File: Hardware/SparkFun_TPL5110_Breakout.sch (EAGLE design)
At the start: 1 part

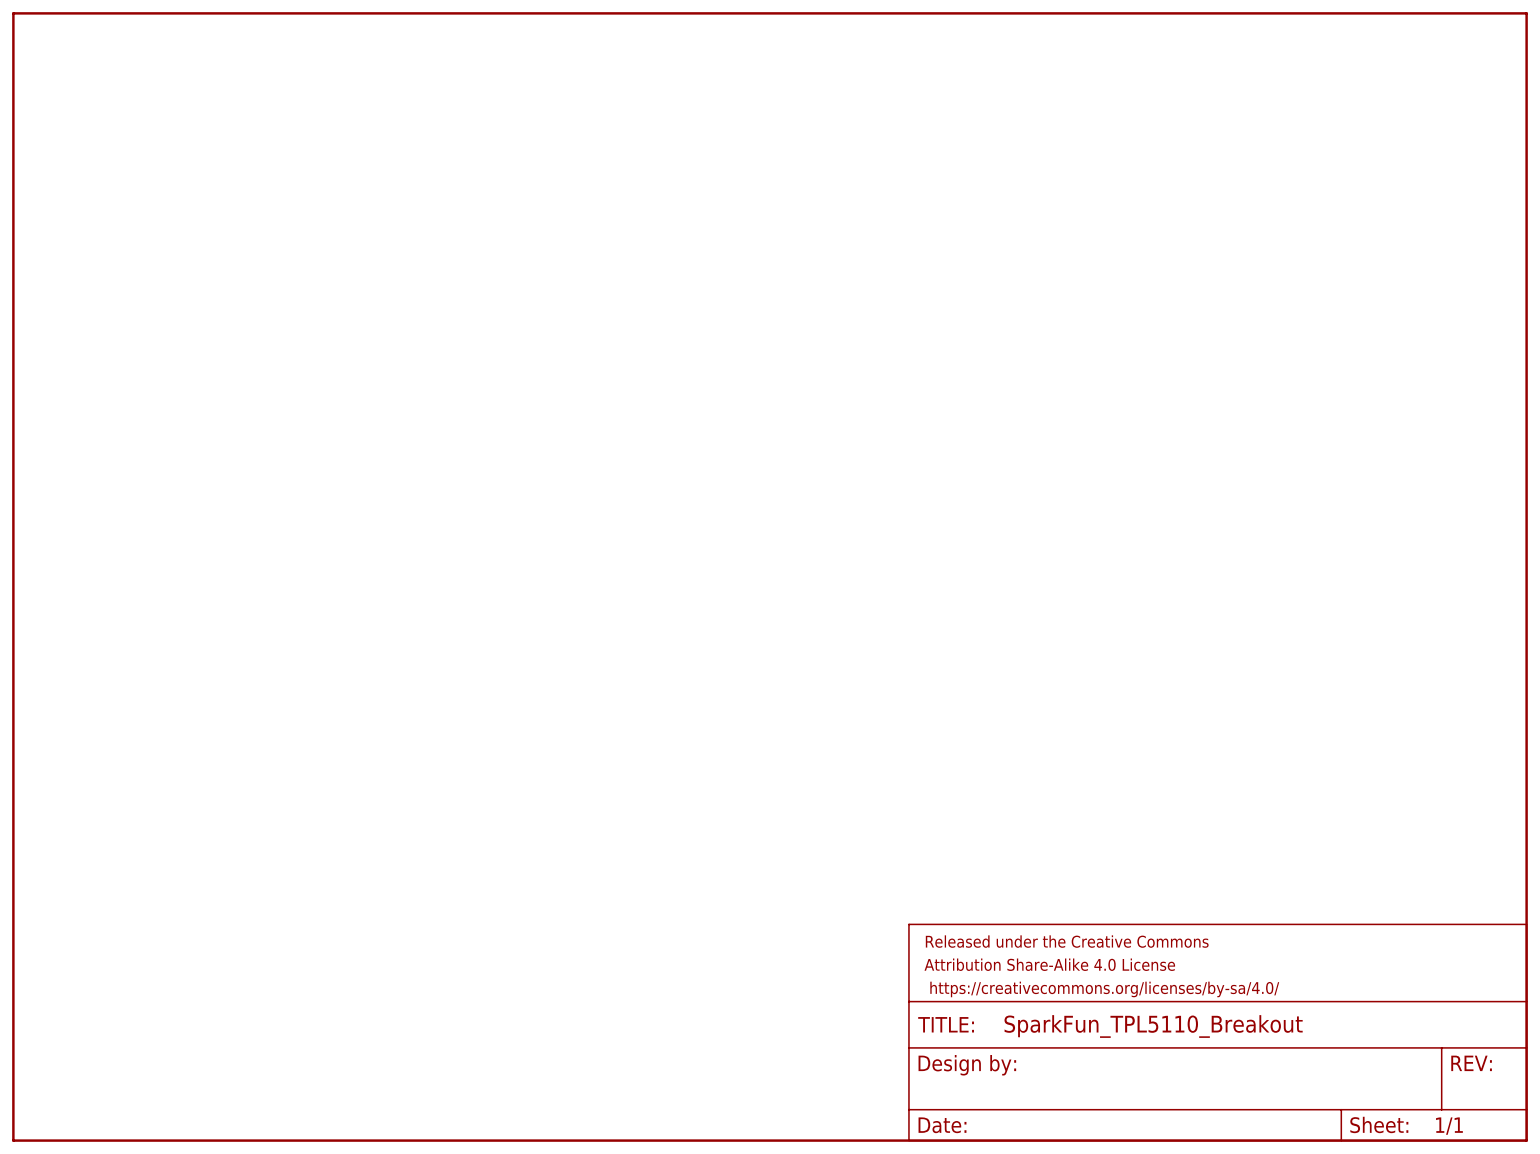
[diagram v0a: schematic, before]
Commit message: Completes schematic and board design, adds buzzard labels
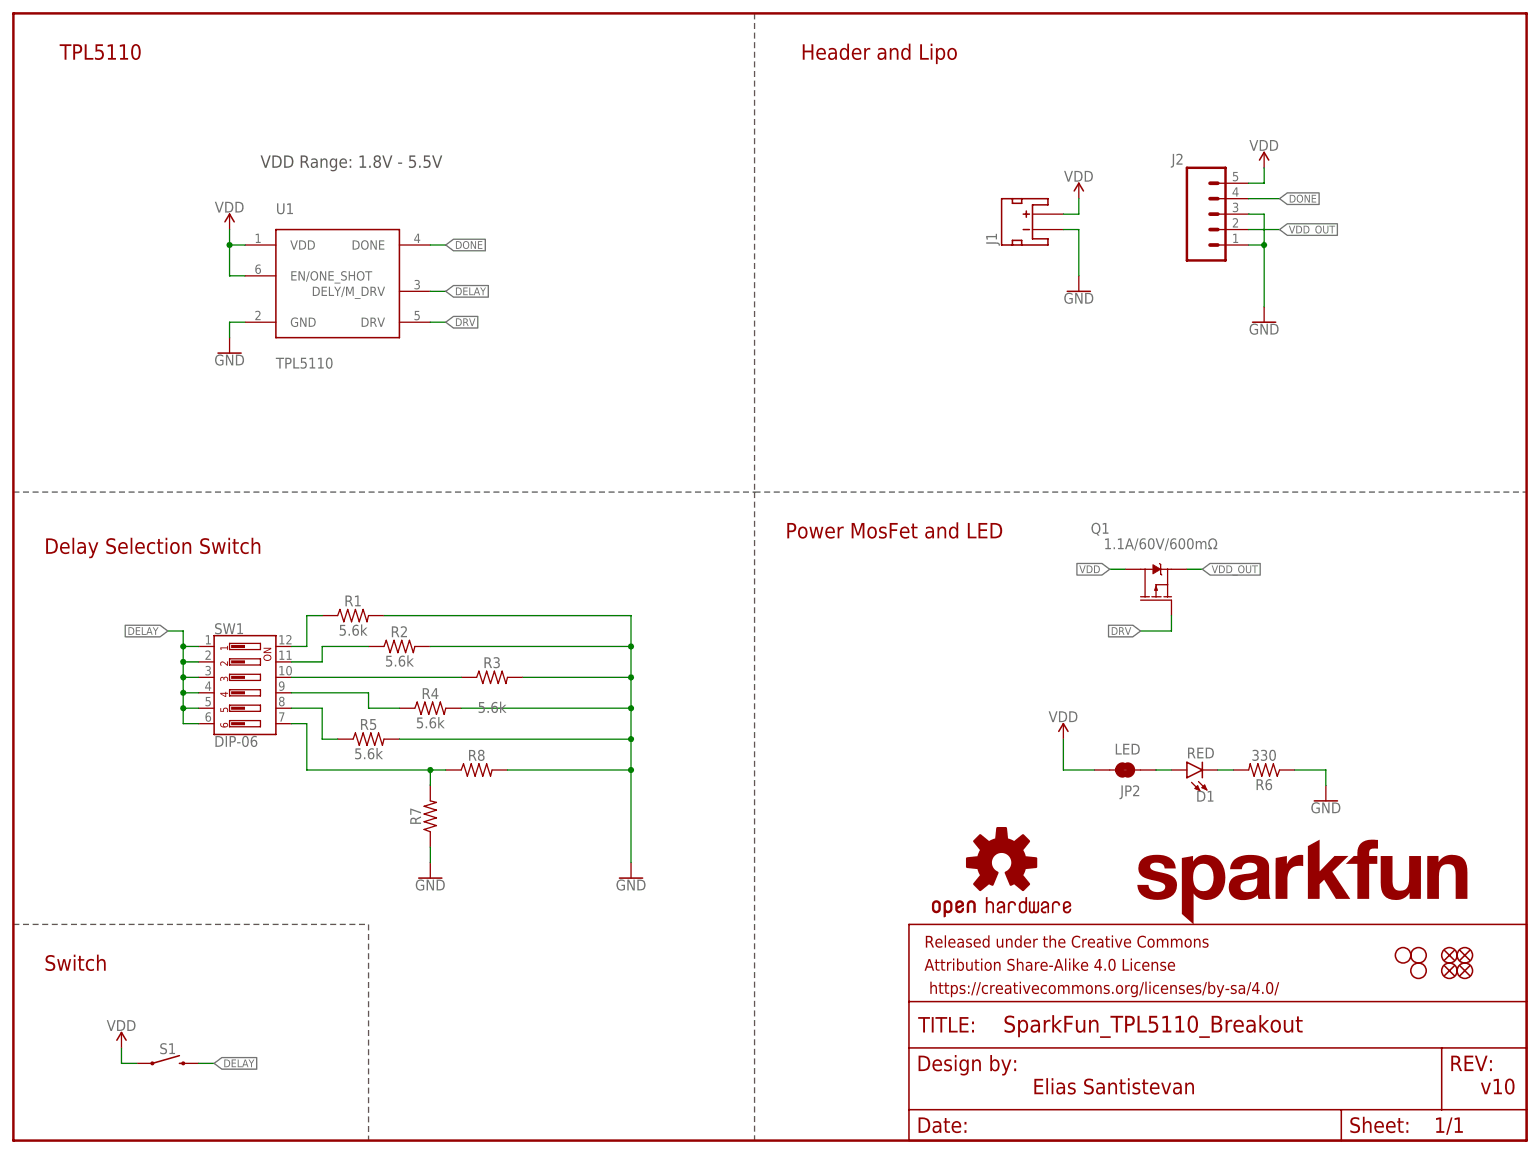
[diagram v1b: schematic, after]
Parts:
- added D1: RED, SparkFun-LED:LED-RED0603
- added FD1, FD2, FD3, FD4: FIDUCIALUFIDUCIAL, SparkFun-Aesthetics:FIDUCIALUFIDUCIAL
- added H1, H2, H4: STAND-OFFTIGHT, SparkFun-Hardware:STAND-OFFTIGHT
- added J1: (no value), SparkFun-Connectors:JST_2MM_MALE
- added J2: (no value), SparkFun-Connectors:CONN_05NO_SILK
- added JP2: LED, SparkFun-Jumpers:JUMPER-SMT_2_NC_TRACE_SILK
- added LOGO1: SFE_LOGO_NAME.1_INCH, SparkFun-Aesthetics:SFE_LOGO_NAME.1_INCH
- added LOGO2: OSHW-LOGOS, SparkFun-Aesthetics:OSHW-LOGOS
- added Q1: 1.1A/60V/600mΩ, SparkFun-DiscreteSemi:MOSFET_PCH-SI2309DS
- added R1, R2, R3, R4, R5: 5.6k, SparkFun-Resistors:5.6KOHM-0603-1/10W-1%
- added R6: 330, SparkFun-Resistors:330OHM-0603-1/10W-1%
- added R7: (no value), SparkFun-Resistors:RESISTOR0603
- added R8: (no value), SparkFun-Resistors:RESISTORAXIAL-0.3
- added S1: MOMENTARY-SWITCH-SPST-SMD-5.2MM-TALL, SparkFun-Switches:MOMENTARY-SWITCH-SPST-SMD-5.2MM-TALL
- added SW1: DIP-06, SparkFun-Switches:DIP-06
- added U1: TPL5110, SparkFun-IC-Power:TPL5110
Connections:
- new net DELAY: S1.2, SW1.1, SW1.2, SW1.3, SW1.4, SW1.5, SW1.6, U1.DELY/M_DRV
- new net DONE: J2.4, U1.DONE
- new net DRV: Q1.G, U1.DRV
- new net GND: J1.-, J2.1, J2.3, R1.2, R2.2, R3.2, R4.2, R5.2, R6.1, R7.1, R8.2, U1.GND
- new net N$1: D1.C, R6.2
- new net N$11: D1.A, JP2.1
- new net N$4: R1.1, SW1.12
- new net N$5: R2.1, SW1.11
- new net N$6: R3.1, SW1.10
- new net N$7: R4.1, SW1.9
- new net N$8: R5.1, SW1.8
- new net N$9: R7.2, R8.1, SW1.7
- new net VDD: J1.+, J2.5, JP2.2, Q1.D, S1.1, U1.EN/ONE_SHOT, U1.VDD
- new net VDD_OUT: J2.2, Q1.S
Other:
- note added: "Delay Selection Switch"
- note added: "Elias Santistevan"
- note added: "Header and Lipo"
- note added: "Power MosFet and LED"
- note added: "Switch"
- note added: "TPL5110"
- note added: "VDD Range: 1.8V - 5.5V"
- note added: "v10"

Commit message: Updates buzzard labels, changes 5 pin header to 6 pin
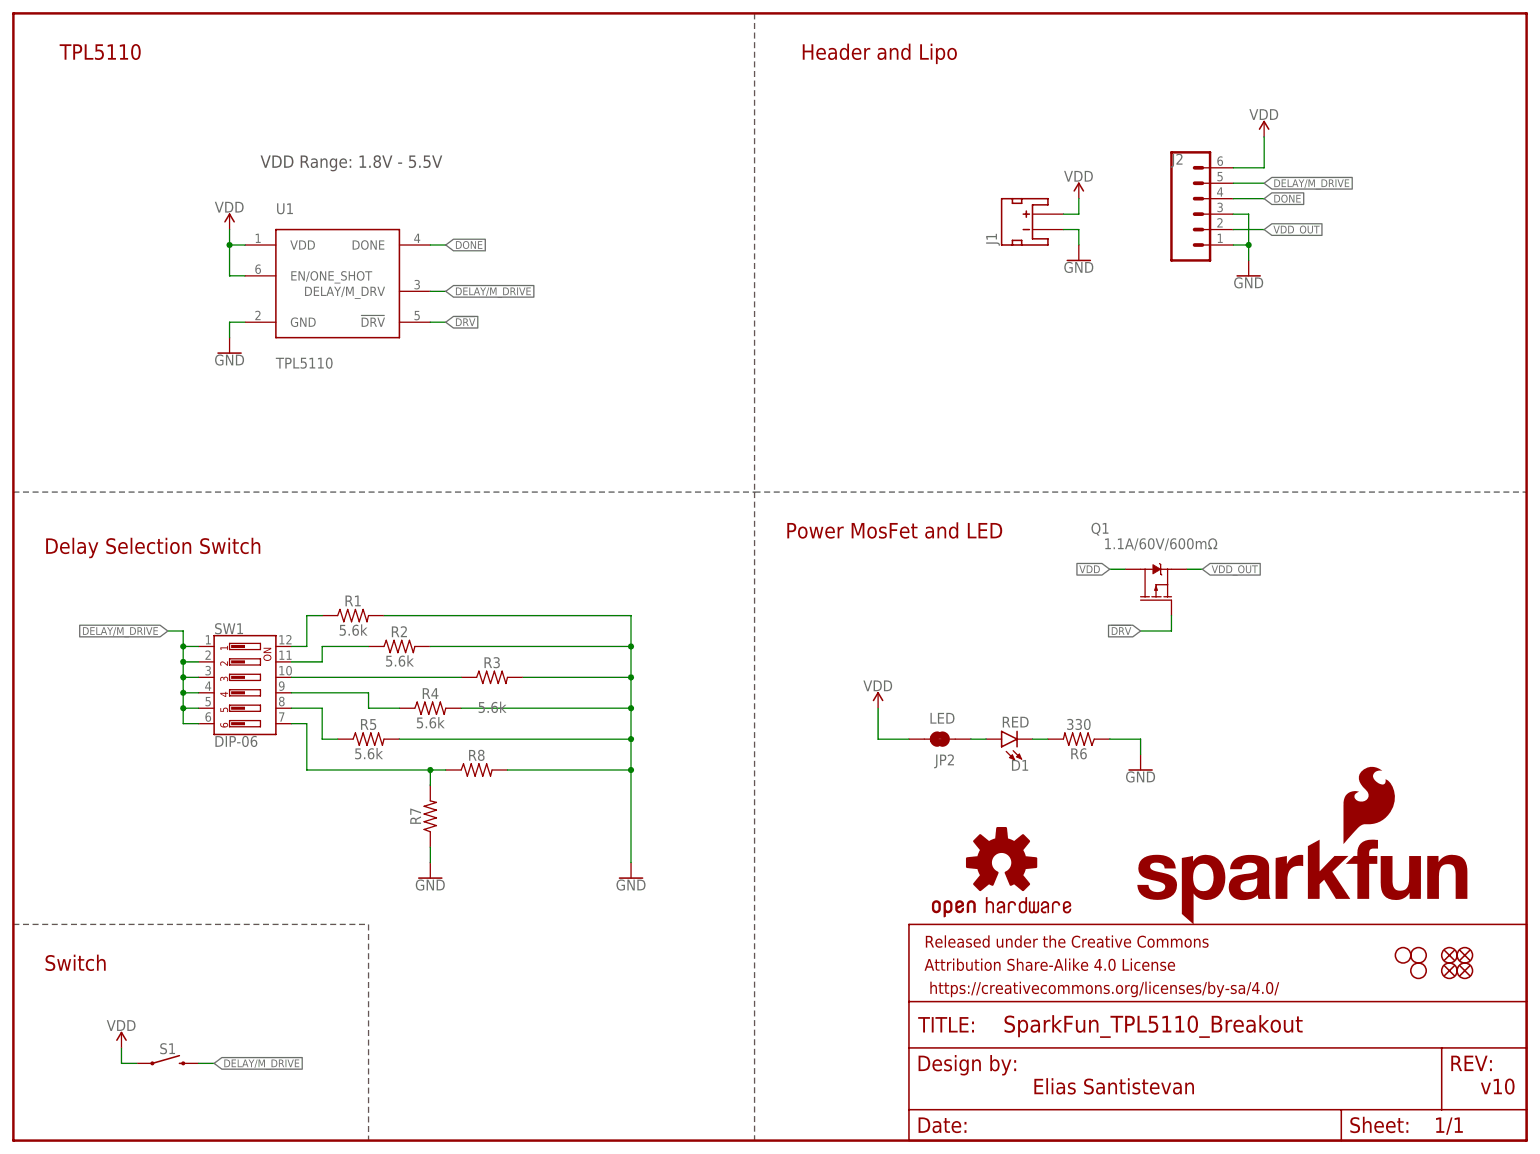
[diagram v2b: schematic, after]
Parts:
- added LOGO3: SFE_LOGO_FLAME.1_INCH, SparkFun-Aesthetics:SFE_LOGO_FLAME.1_INCH
- J2: device SparkFun-Connectors:CONN_05NO_SILK -> SparkFun-Connectors:CONN_06NO_SILK_NO_POP
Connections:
- removed net DELAY: S1.2, SW1.1, SW1.2, SW1.3, SW1.4, SW1.5, SW1.6, U1.DELY/M_DRV
- removed net DRV: Q1.G, U1.DRV
- new net !DRV: Q1.G, U1.!DRV
- new net DELAY/M_DRIVE: J2.5, S1.2, SW1.1, SW1.2, SW1.3, SW1.4, SW1.5, SW1.6, U1.DELAY/M_DRV
- net VDD: now also J2.6; no longer J2.5
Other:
- moved on the sheet: D1, JP2, R6

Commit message: Alignes swtich silk, adds "in/out" silk, increases size of product name silk
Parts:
- R1: value 5.6k -> 16.2k; device SparkFun-Resistors:5.6KOHM-0603-1/10W-1% -> SparkFun-Resistors:16.2KOHM-0603-1/10W-1%
- R2: value 5.6k -> 22k; device SparkFun-Resistors:5.6KOHM-0603-1/10W-1% -> SparkFun-Resistors:22KOHM-0603-1/10W-1%
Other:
- note added: "92k, 125k, 170k"
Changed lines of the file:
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@@
 <part name="U1" library="SparkFun-IC-Power" deviceset="TPL5110" device=""/>
 <part name="S1" library="SparkFun-Switches" deviceset="MOMENTARY-SWITCH-SPST" device="-SMD-5.2MM-TALL"/>
-<part name="R1" library="SparkFun-Resistors" deviceset="5.6KOHM" device="-0603-1/10W-1%" value="5.6k"/>
-<part name="R2" library="SparkFun-Resistors" deviceset="5.6KOHM" device="-0603-1/10W-1%" value="5.6k"/>
+<part name="R1" library="SparkFun-Resistors" deviceset="16.2KOHM" device="-0603-1/10W-1%" value="16.2k"/>
+<part name="R2" library="SparkFun-Resistors" deviceset="22KOHM" device="-0603-1/10W-1%" value="22k"/>
 <part name="R3" library="SparkFun-Resistors" deviceset="5.6KOHM" device="-0603-1/10W-1%" value="5.6k"/>
 <part name="R4" library="SparkFun-Resistors" deviceset="5.6KOHM" device="-0603-1/10W-1%" value="5.6k"/>
@@
 <wire x1="58.42" y1="35.56" x2="58.42" y2="0" width="0.2032" layer="97" style="shortdash"/>
 <text x="5.08" y="27.94" size="2.54" layer="94" font="vector">Switch</text>
+<text x="86.36" y="78.74" size="2.032" layer="91" font="vector">92k, 125k, 170k</text>
 </plain>
 <instances>

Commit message: Adds final resistor values: 93.1k, 124k, 169k, Updates python script so that user can calculate combinations with 6th custom resistor
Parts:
- R3: value 5.6k -> 93.1k; device SparkFun-Resistors:5.6KOHM-0603-1/10W-1% -> SparkFun-Resistors:93.1KOHM
- R4: value 5.6k -> 124k; device SparkFun-Resistors:5.6KOHM-0603-1/10W-1% -> SparkFun-Resistors:124KOHM
- R5: value 5.6k -> 169K; device SparkFun-Resistors:5.6KOHM-0603-1/10W-1% -> SparkFun-Resistors:169KOHM
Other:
- note added: "Disable"
- note removed: "92k, 125k, 170k"
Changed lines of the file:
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@@
 <part name="R1" library="SparkFun-Resistors" deviceset="16.2KOHM" device="-0603-1/10W-1%" value="16.2k"/>
 <part name="R2" library="SparkFun-Resistors" deviceset="22KOHM" device="-0603-1/10W-1%" value="22k"/>
-<part name="R3" library="SparkFun-Resistors" deviceset="5.6KOHM" device="-0603-1/10W-1%" value="5.6k"/>
-<part name="R4" library="SparkFun-Resistors" deviceset="5.6KOHM" device="-0603-1/10W-1%" value="5.6k"/>
-<part name="R5" library="SparkFun-Resistors" deviceset="5.6KOHM" device="-0603-1/10W-1%" value="5.6k"/>
+<part name="R4" library="SparkFun-Resistors" deviceset="124KOHM" device="" value="124k"/>
+<part name="R5" library="SparkFun-Resistors" deviceset="169KOHM" device="" value="169K"/>
 <part name="R6" library="SparkFun-Resistors" deviceset="330OHM" device="-0603-1/10W-1%" value="330"/>
 <part name="D1" library="SparkFun-LED" deviceset="LED-RED" device="0603" value="RED"/>
@@
 <part name="LOGO2" library="SparkFun-Aesthetics" deviceset="OSHW-LOGO" device="S"/>
 <part name="LOGO3" library="SparkFun-Aesthetics" deviceset="SFE_LOGO_FLAME" device=".1_INCH"/>
+<part name="R3" library="SparkFun-Resistors" deviceset="93.1KOHM" device="" value="93.1k"/>
 </parts>
 <sheets>
@@
 <wire x1="58.42" y1="35.56" x2="58.42" y2="0" width="0.2032" layer="97" style="shortdash"/>
 <text x="5.08" y="27.94" size="2.54" layer="94" font="vector">Switch</text>
-<text x="86.36" y="78.74" size="2.032" layer="91" font="vector">92k, 125k, 170k</text>
+<text x="149.86" y="71.12" size="2.032" layer="97" font="vector">Disable</text>
 </plain>
 <instances>
@@
 <attribute name="VALUE" x="63.5" y="79.756" size="1.778" layer="96" font="vector" align="top-center"/>
 </instance>
-<instance part="R3" gate="G$1" x="78.74" y="76.2" smashed="yes">
-<attribute name="NAME" x="78.74" y="77.724" size="1.778" layer="95" font="vector" align="bottom-center"/>
-<attribute name="VALUE" x="78.74" y="72.136" size="1.778" layer="96" font="vector" align="top-center"/>
-</instance>
 <instance part="R4" gate="G$1" x="68.58" y="71.12" smashed="yes">
 <attribute name="NAME" x="68.58" y="72.644" size="1.778" layer="95" font="vector" align="bottom-center"/>
@@
 <instance part="LOGO2" gate="G$1" x="162.56" y="45.72" smashed="yes"/>
 <instance part="LOGO3" gate="G$1" x="218.44" y="48.26" smashed="yes"/>
+<instance part="R3" gate="G$1" x="78.74" y="76.2" smashed="yes">
+<attribute name="NAME" x="78.74" y="77.724" size="1.778" layer="95" font="vector" align="bottom-center"/>
+<attribute name="VALUE" x="78.74" y="74.676" size="1.778" layer="96" font="vector" align="top-center"/>
+</instance>
 </instances>
 <busses>
@@
 <wire x1="68.58" y1="81.28" x2="101.6" y2="81.28" width="0.1524" layer="91"/>
 <junction x="101.6" y="81.28"/>
-<pinref part="R3" gate="G$1" pin="2"/>
 <wire x1="83.82" y1="76.2" x2="101.6" y2="76.2" width="0.1524" layer="91"/>
 <junction x="101.6" y="76.2"/>
@@
 <wire x1="81.28" y1="60.96" x2="101.6" y2="60.96" width="0.1524" layer="91"/>
 <junction x="101.6" y="60.96"/>
+<pinref part="R3" gate="G$1" pin="2"/>
 </segment>
 <segment>
@@
 <net name="N$6" class="0">
 <segment>
-<pinref part="R3" gate="G$1" pin="1"/>
 <pinref part="SW1" gate="G$1" pin="10"/>
 <wire x1="73.66" y1="76.2" x2="45.72" y2="76.2" width="0.1524" layer="91"/>
-</segment>
-</net>
+<pinref part="R3" gate="G$1" pin="1"/>
+</segment>
+</net>

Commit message: Adds Production Files and adds text to custom resistors
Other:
- note added: "Custom Value Resistors"
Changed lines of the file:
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@@
 <text x="5.08" y="27.94" size="2.54" layer="94" font="vector">Switch</text>
 <text x="149.86" y="71.12" size="2.032" layer="97" font="vector">Disable</text>
+<text x="73.66" y="53.34" size="1.778" layer="97" font="vector">Custom Value Resistors</text>
 </plain>
 <instances>
@@
 <attribute name="VALUE" x="185.42" y="60.706" size="1.778" layer="96" align="top-center"/>
 </instance>
-<instance part="SUPPLY3" gate="VDD" x="142.24" y="71.12" smashed="yes">
-<attribute name="VALUE" x="142.24" y="73.914" size="1.778" layer="96" align="bottom-center"/>
+<instance part="SUPPLY3" gate="VDD" x="144.78" y="68.58" smashed="yes">
+<attribute name="VALUE" x="144.78" y="71.374" size="1.778" layer="96" align="bottom-center"/>
 </instance>
 <instance part="H1" gate="G$1" x="231.14" y="30.48" smashed="yes"/>
 <instance part="H2" gate="G$1" x="231.14" y="27.94" smashed="yes"/>
 <instance part="H4" gate="G$1" x="228.6" y="30.48" smashed="yes"/>
-<instance part="SUPPLY4" gate="VDD" x="205.74" y="165.1" smashed="yes">
-<attribute name="VALUE" x="205.74" y="167.894" size="1.778" layer="96" align="bottom-center"/>
+<instance part="SUPPLY4" gate="VDD" x="203.2" y="162.56" smashed="yes">
+<attribute name="VALUE" x="203.2" y="165.354" size="1.778" layer="96" align="bottom-center"/>
 </instance>
 <instance part="SUPPLY5" gate="VDD" x="17.78" y="15.24" smashed="yes">
@@
 <pinref part="SUPPLY3" gate="VDD" pin="VDD"/>
 <pinref part="JP2" gate="G$1" pin="2"/>
-<wire x1="142.24" y1="71.12" x2="142.24" y2="66.04" width="0.1524" layer="91"/>
-<wire x1="142.24" y1="66.04" x2="147.32" y2="66.04" width="0.1524" layer="91"/>
+<wire x1="144.78" y1="68.58" x2="144.78" y2="66.04" width="0.1524" layer="91"/>
+<wire x1="144.78" y1="66.04" x2="147.32" y2="66.04" width="0.1524" layer="91"/>
 </segment>
 <segment>
@@
 <pinref part="SUPPLY4" gate="VDD" pin="VDD"/>
 <pinref part="J2" gate="G$1" pin="6"/>
-<wire x1="205.74" y1="160.02" x2="205.74" y2="165.1" width="0.1524" layer="91"/>
-<wire x1="200.66" y1="160.02" x2="205.74" y2="160.02" width="0.1524" layer="91"/>
+<wire x1="203.2" y1="160.02" x2="203.2" y2="162.56" width="0.1524" layer="91"/>
+<wire x1="200.66" y1="160.02" x2="203.2" y2="160.02" width="0.1524" layer="91"/>
 </segment>
 </net>
